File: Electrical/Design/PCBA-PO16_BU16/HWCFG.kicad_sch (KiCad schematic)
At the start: 4 parts, among them U801 74HC165

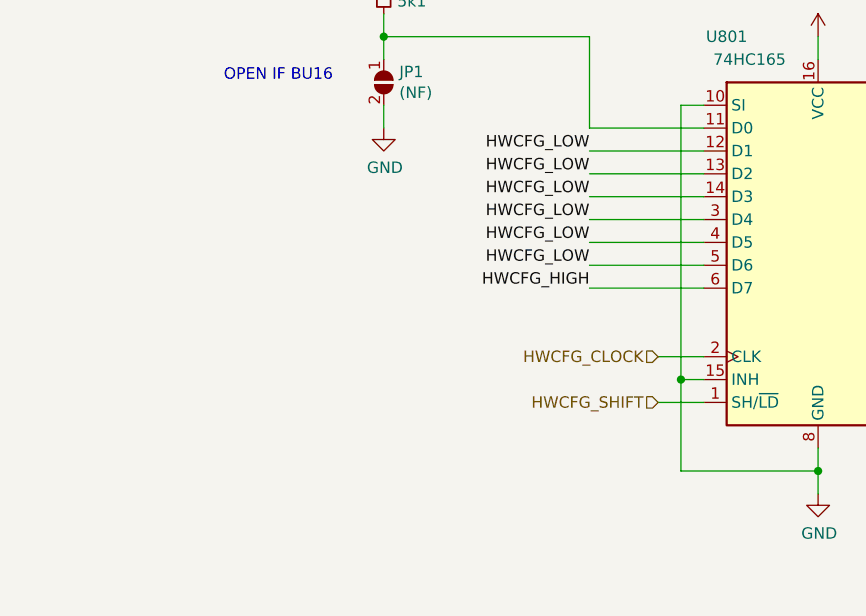
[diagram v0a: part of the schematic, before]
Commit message: SUKU hwcfg updated to allow PB44
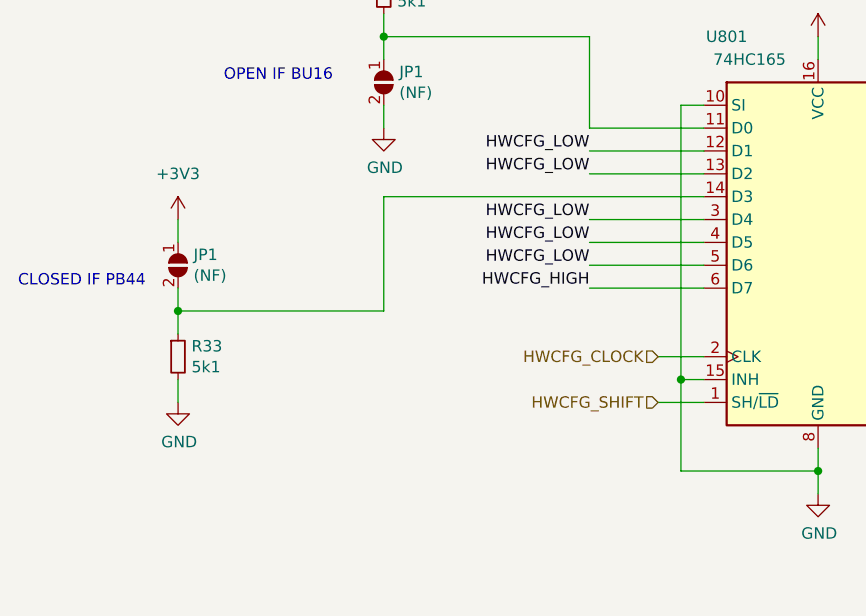
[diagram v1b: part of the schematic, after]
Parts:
- added JP1: (NF), Jumper:SolderJumper-2_P1.3mm_Open_TrianglePad1.0x1.5mm, symbol suku_basics:JP_SolderJumper_2_Open
- added R33: 5k1, suku_basics:RES_0402, symbol suku_basics:RES
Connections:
- net +3V3: now also JP1.1 (A)
- net GND: now also R33.2; no longer U801.14 (D3)
- new net: JP1.2 (B), R33.1, U801.14 (D3)
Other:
- note added: "CLOSED IF PB44"
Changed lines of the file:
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@@
 (kicad_sch (version 20230121) (generator eeschema)
   (paper "A4")
+  (junction (at 33.02 93.98) (diameter 0) (color 0 0 0 0)
+  )
   (junction (at 104.14 111.76) (diameter 0) (color 0 0 0 0)
   )
@@
   )
   (no_connect (at 116.84 73.66))
+  (wire (pts (xy 33.02 91.44) (xy 33.02 93.98))
+    (stroke (width 0) (type default))
+  )
+  (wire (pts (xy 33.02 93.98) (xy 33.02 96.52))
+    (stroke (width 0) (type default))
+  )
   (wire (pts (xy 88.9 71.12) (xy 88.9 101.6))
     (stroke (width 0) (type default))
@@
     (stroke (width 0) (type default))
   )
+  (wire (pts (xy 55.88 81.28) (xy 91.44 81.28))
+    (stroke (width 0) (type default))
+  )
   (wire (pts (xy 78.74 73.66) (xy 78.74 63.5))
     (stroke (width 0) (type default))
   )
+  (wire (pts (xy 33.02 83.82) (xy 33.02 86.36))
+    (stroke (width 0) (type default))
+  )
   (wire (pts (xy 91.44 101.6) (xy 88.9 101.6))
     (stroke (width 0) (type default))
@@
     (stroke (width 0) (type default))
   )
+  (wire (pts (xy 55.88 93.98) (xy 33.02 93.98))
+    (stroke (width 0) (type default))
+  )
   (wire (pts (xy 91.44 76.2) (xy 78.74 76.2))
     (stroke (width 0) (type default))
@@
     (stroke (width 0) (type default))
   )
+  (wire (pts (xy 55.88 81.28) (xy 55.88 93.98))
+    (stroke (width 0) (type default))
+  )
   (wire (pts (xy 78.74 91.44) (xy 91.44 91.44))
     (stroke (width 0) (type default))
@@
     (stroke (width 0) (type default))
   )
+  (wire (pts (xy 33.02 104.14) (xy 33.02 101.6))
+    (stroke (width 0) (type default))
+  )
   (wire (pts (xy 121.92 88.9) (xy 121.92 91.44))
     (stroke (width 0) (type default))
   )
   (wire (pts (xy 88.9 111.76) (xy 104.14 111.76))
-    (stroke (width 0) (type default))
-  )
-  (wire (pts (xy 91.44 81.28) (xy 78.74 81.28))
     (stroke (width 0) (type default))
   )
@@
     (effects (font (size 1.27 1.27)) (justify left bottom))
   )
+  (text "CLOSED IF PB44" (at 15.24 91.44 0)
+    (effects (font (size 1.27 1.27)) (justify left bottom))
+  )
   (text "OPEN IF BU16" (at 38.1 68.58 0)
     (effects (font (size 1.27 1.27)) (justify left bottom))
@@
   )
   (label "HWCFG_LOW" (at 78.74 86.36 180) (fields_autoplaced)
-    (effects (font (size 1.27 1.27)) (justify right bottom))
-  )
-  (label "HWCFG_LOW" (at 78.74 81.28 180) (fields_autoplaced)
     (effects (font (size 1.27 1.27)) (justify right bottom))
   )
@@
     (pin "7")
     (instances
-      (project "PO16_BU16"
+      (project "PCBA-PO16_BU16"
         (path "/e5217a0c-7f55-4c30-adda-7f8d95709d1b/00000000-0000-0000-0000-00005dc2dc06"
           (reference "U801") (unit 1)
@@
     (pin "1")
     (instances
-      (project "PO16_BU16"
+      (project "PCBA-PO16_BU16"
         (path "/e5217a0c-7f55-4c30-adda-7f8d95709d1b/00000000-0000-0000-0000-00005dc2dc06"
           (reference "#PWR0882") (unit 1)
@@
     (pin "2")
     (instances
-      (project "PO16_BU16"
+      (project "PCBA-PO16_BU16"
         (path "/e5217a0c-7f55-4c30-adda-7f8d95709d1b/00000000-0000-0000-0000-00005dc2dc06"
           (reference "C801") (unit 1)
@@
     (pin "1")
     (instances
-      (project "PO16_BU16"
+      (project "PCBA-PO16_BU16"
         (path "/e5217a0c-7f55-4c30-adda-7f8d95709d1b/00000000-0000-0000-0000-00005dc2dc06"
           (reference "#PWR0943") (unit 1)
@@
     (pin "1")
     (instances
-      (project "PO16_BU16"
+      (project "PCBA-PO16_BU16"
         (path "/e5217a0c-7f55-4c30-adda-7f8d95709d1b/00000000-0000-0000-0000-00005dc2dc06"
           (reference "#PWR0881") (unit 1)
+        )
+      )
+    )
+  )
+  (symbol (lib_id "power:+3V3") (at 33.02 83.82 0) (unit 1)
+    (in_bom yes) (on_board yes) (dnp no) (fields_autoplaced)
+    (property "Reference" "#PWR0701" (at 33.02 87.63 0)
+      (effects (font (size 1.27 1.27)) hide)
+    )
+    (property "Value" "+3V3" (at 33.02 78.74 0)
+      (effects (font (size 1.27 1.27)))
+    )
+    (property "Footprint" "" (at 33.02 83.82 0)
+      (effects (font (size 1.27 1.27)) hide)
+    )
+    (property "Datasheet" "" (at 33.02 83.82 0)
+      (effects (font (size 1.27 1.27)) hide)
+    )
+    (pin "1")
+    (instances
+      (project "PCBA-PO16_BU16"
+        (path "/e5217a0c-7f55-4c30-adda-7f8d95709d1b/00000000-0000-0000-0000-00005dc2dc06"
+          (reference "#PWR0701") (unit 1)
+        )
+      )
+    )
+  )
+  (symbol (lib_id "suku_basics:JP_SolderJumper_2_Open") (at 33.02 88.9 270) (unit 1)
+    (in_bom yes) (on_board yes) (dnp no)
+    (property "Reference" "JP1" (at 34.7472 87.7316 90)
+      (effects (font (size 1.27 1.27)) (justify left))
+    )
+    (property "Value" "(NF)" (at 34.7472 90.043 90)
+      (effects (font (size 1.27 1.27)) (justify left))
+    )
+    (property "Footprint" "Jumper:SolderJumper-2_P1.3mm_Open_TrianglePad1.0x1.5mm" (at 33.02 88.9 0)
+      (effects (font (size 1.27 1.27)) hide)
+    )
+    (property "Datasheet" "~" (at 33.02 88.9 0)
+      (effects (font (size 1.27 1.27)) hide)
+    )
+    (pin "1")
+    (pin "2")
+    (instances
+      (project "HWCFG"
+        (path "/dbe92a0d-89cb-4d3f-9497-c2c1d93a3018"
+          (reference "JP1") (unit 1)
+        )
+      )
+      (project "PCBA-PO16_BU16"
+        (path "/e5217a0c-7f55-4c30-adda-7f8d95709d1b/00000000-0000-0000-0000-00005dc2dc06"
+          (reference "JP701") (unit 1)
         )
       )
@@
         )
       )
-      (project "PO16_BU16"
+      (project "PCBA-PO16_BU16"
         (path "/e5217a0c-7f55-4c30-adda-7f8d95709d1b/00000000-0000-0000-0000-00005dc2dc06"
           (reference "#PWR0880") (unit 1)
@@
     (pin "1")
     (instances
-      (project "PO16_BU16"
+      (project "PCBA-PO16_BU16"
         (path "/e5217a0c-7f55-4c30-adda-7f8d95709d1b/00000000-0000-0000-0000-00005dc2dc06"
           (reference "#PWR0879") (unit 1)
+        )
+      )
+    )
+  )
+  (symbol (lib_id "power:GND") (at 33.02 104.14 0) (unit 1)
+    (in_bom yes) (on_board yes) (dnp no)
+    (property "Reference" "#PWR0152" (at 33.02 110.49 0)
+      (effects (font (size 1.27 1.27)) hide)
+    )
+    (property "Value" "GND" (at 33.147 108.5342 0)
+      (effects (font (size 1.27 1.27)))
+    )
+    (property "Footprint" "" (at 33.02 104.14 0)
+      (effects (font (size 1.27 1.27)) hide)
+    )
+    (property "Datasheet" "" (at 33.02 104.14 0)
+      (effects (font (size 1.27 1.27)) hide)
+    )
+    (pin "1")
+    (instances
+      (project "HWCFG"
+        (path "/dbe92a0d-89cb-4d3f-9497-c2c1d93a3018"
+          (reference "#PWR0152") (unit 1)
+        )
+      )
+      (project "PCBA-PO16_BU16"
+        (path "/e5217a0c-7f55-4c30-adda-7f8d95709d1b/00000000-0000-0000-0000-00005dc2dc06"
+          (reference "#PWR0702") (unit 1)
         )
       )
@@
         )
       )
-      (project "PO16_BU16"
+      (project "PCBA-PO16_BU16"
         (path "/e5217a0c-7f55-4c30-adda-7f8d95709d1b/00000000-0000-0000-0000-00005dc2dc06"
           (reference "R801") (unit 1)
+        )
+      )
+    )
+  )
+  (symbol (lib_id "suku_basics:RES") (at 33.02 99.06 0) (unit 1)
+    (in_bom yes) (on_board yes) (dnp no)
+    (property "Reference" "R33" (at 34.5186 97.8916 0)
+      (effects (font (size 1.27 1.27)) (justify left))
+    )
+    (property "Value" "5k1" (at 34.5186 100.203 0)
+      (effects (font (size 1.27 1.27)) (justify left))
+    )
+    (property "Footprint" "suku_basics:RES_0402" (at 33.02 99.06 0)
+      (effects (font (size 1.27 1.27)) hide)
+    )
+    (property "Datasheet" "~" (at 33.02 99.06 0)
+      (effects (font (size 1.27 1.27)) hide)
+    )
+    (pin "1")
+    (pin "2")
+    (instances
+      (project "HWCFG"
+        (path "/dbe92a0d-89cb-4d3f-9497-c2c1d93a3018"
+          (reference "R33") (unit 1)
+        )
+      )
+      (project "PCBA-PO16_BU16"
+        (path "/e5217a0c-7f55-4c30-adda-7f8d95709d1b/00000000-0000-0000-0000-00005dc2dc06"
+          (reference "R702") (unit 1)
         )
       )
@@
     (pin "1")
     (instances
-      (project "PO16_BU16"
+      (project "PCBA-PO16_BU16"
         (path "/e5217a0c-7f55-4c30-adda-7f8d95709d1b/00000000-0000-0000-0000-00005dc2dc06"
           (reference "#PWR0942") (unit 1)
@@
         )
       )
-      (project "PO16_BU16"
+      (project "PCBA-PO16_BU16"
         (path "/e5217a0c-7f55-4c30-adda-7f8d95709d1b/00000000-0000-0000-0000-00005dc2dc06"
           (reference "JP801") (unit 1)

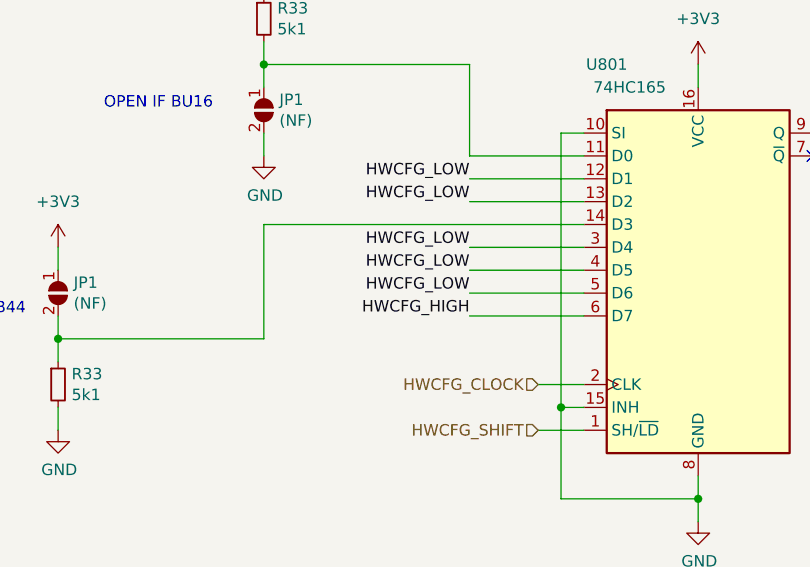
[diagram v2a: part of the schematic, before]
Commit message: SUKU new mux pinout implemented, hwcfg updated accordingly
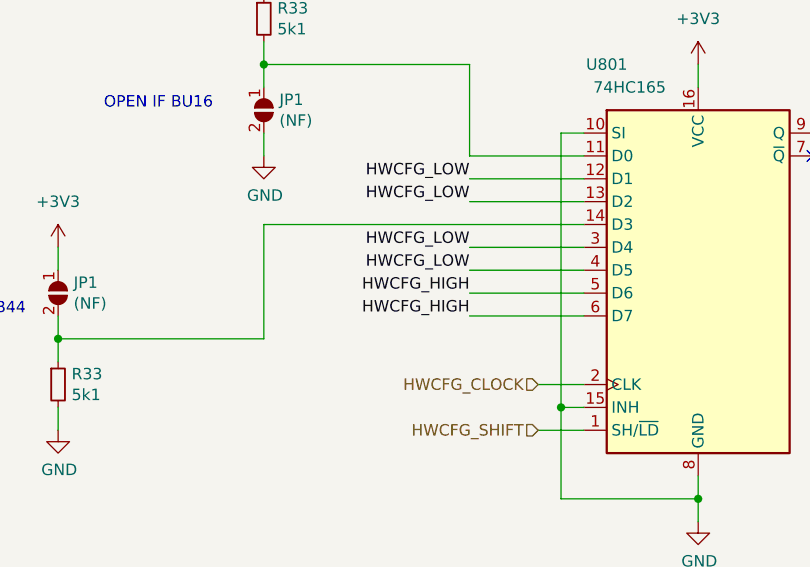
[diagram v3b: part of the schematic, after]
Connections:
- net +3V3: now also U801.5 (D6)
- net GND: no longer U801.5 (D6)
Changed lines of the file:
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@@
+		)
+	)
+	(label "HWCFG_HIGH"
+		(at 78.74 88.9 180)
+		(fields_autoplaced yes)
+		(effects
+			(font
+				(size 1.27 1.27)
+			)
+			(justify right bottom)
 		)
 	)
@@
 		(fields_autoplaced yes)
 		(effects
-			(font
-				(size 1.27 1.27)
-			)
-			(justify right bottom)
-		)
-	)
-	(label "HWCFG_LOW"
-		(at 78.74 88.9 180)
-		(fields_autoplaced yes)
-		(effects
